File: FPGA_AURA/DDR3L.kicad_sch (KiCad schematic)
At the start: 58 parts, among them U500 MT41K128M16JT-125_IT_K

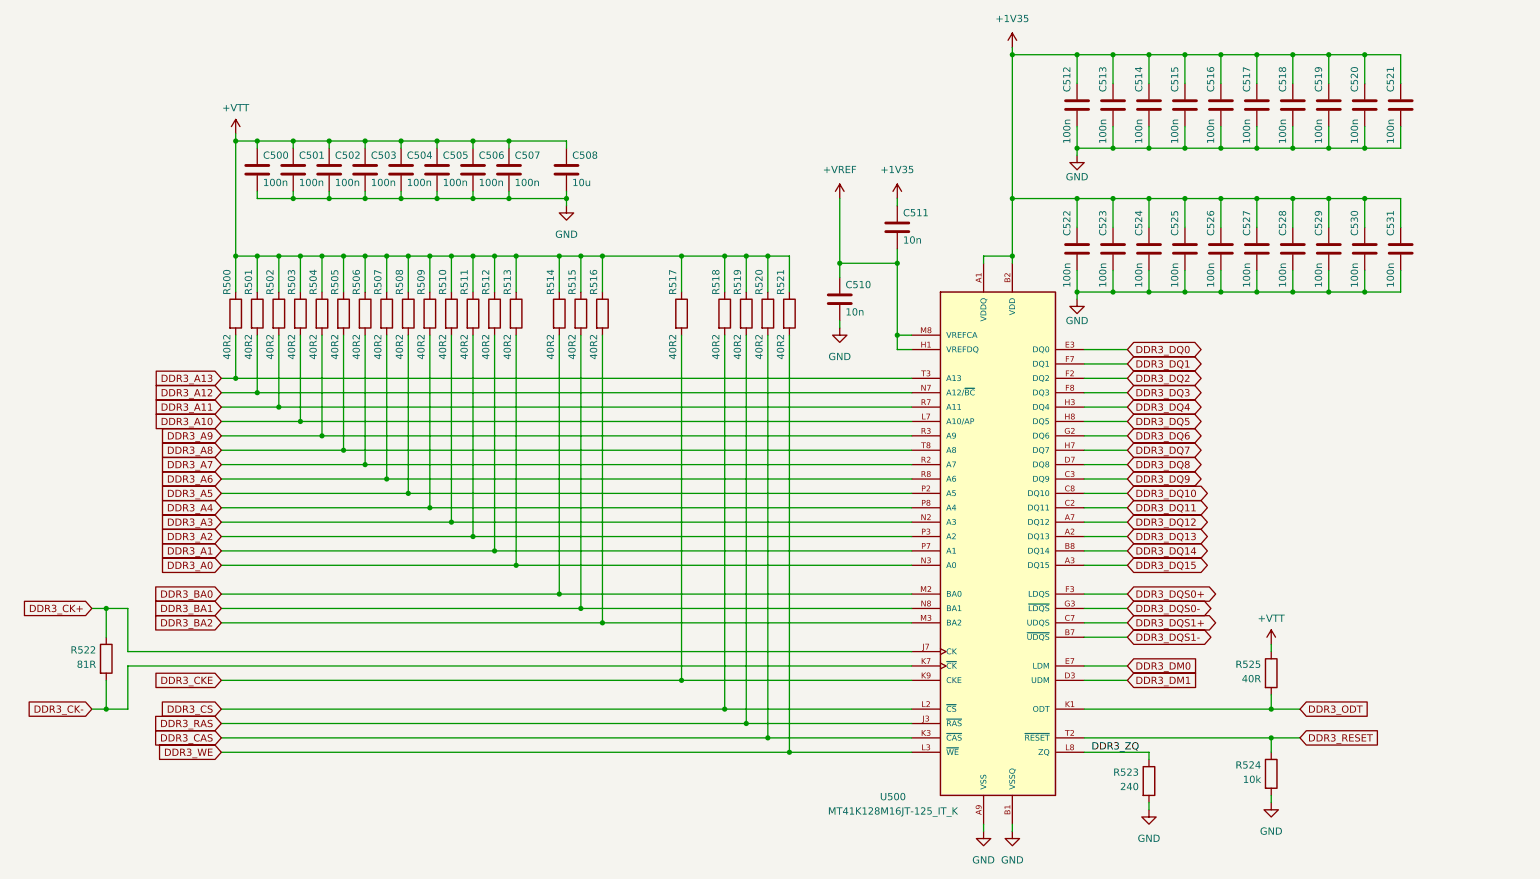
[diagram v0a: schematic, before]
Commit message: Following new DDR3 reference
Using Scopefun v2 as a reference design for the XC7A35T-FTG256
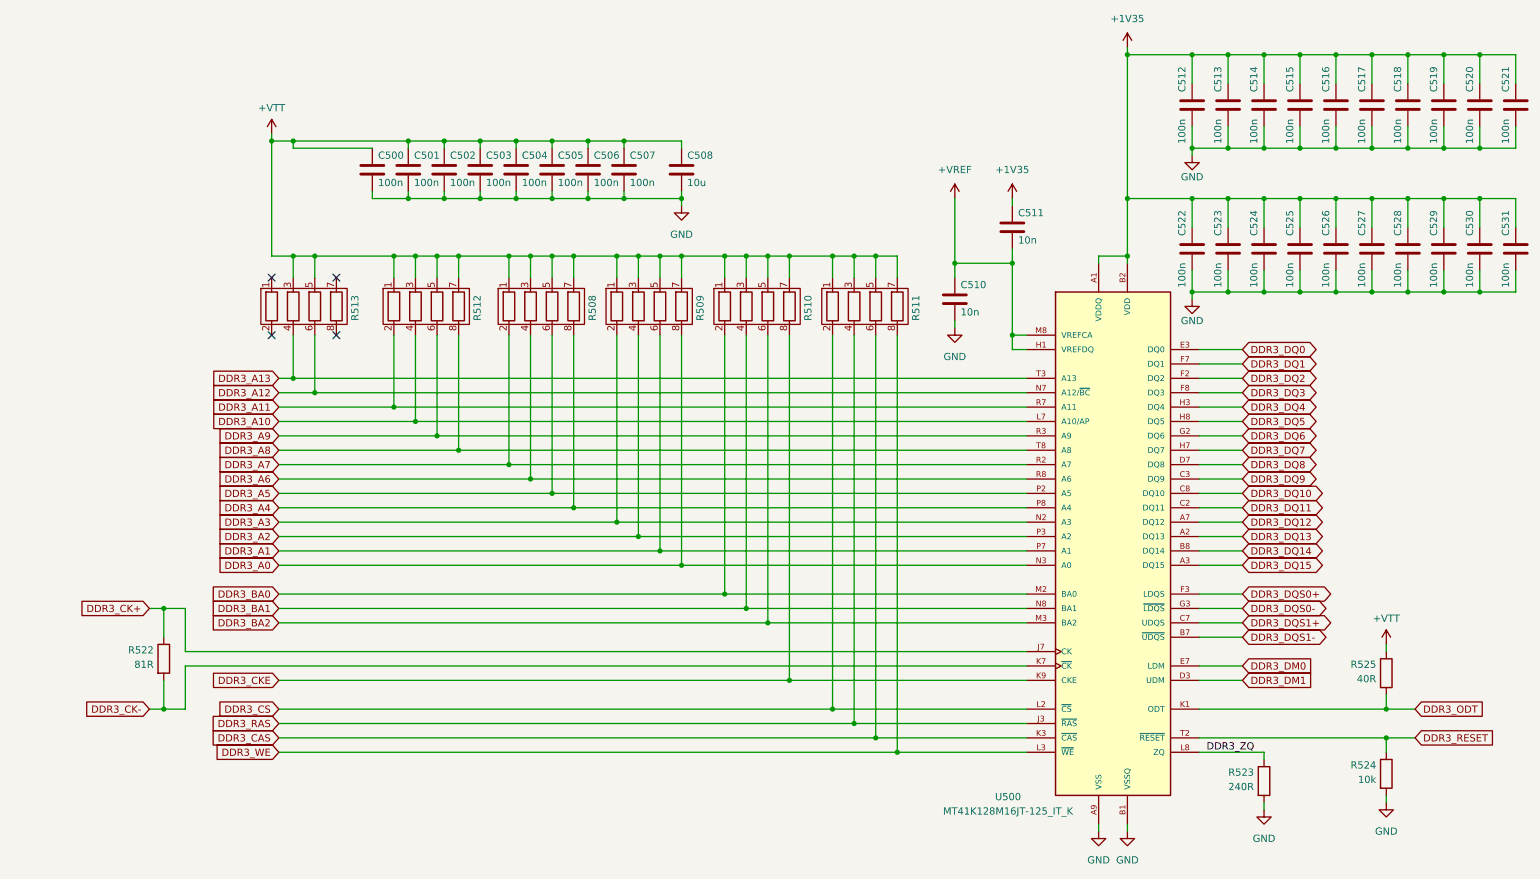
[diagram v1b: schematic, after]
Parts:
- removed R500, R501, R502, R503, R504, R505, R506, R507, R508, R509, R510, R511, R512, R513, R514, R515, R516, R517, R518, R519, R520, R521: 40R2, Resistor_SMD:R_0402_1005Metric, symbol Device:R
- added R508, R509, R510, R511, R512, R513: ~, YC124-FR-0740R2L:0402_4, symbol YC124-FR-0740R2L:R_Array
- R523: value 240 -> 240R
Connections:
- net +VTT: now also R508.1, R508.3, R508.5, R508.7, R509.1, R509.3, R509.5, R509.7, R510.1, R510.3, R510.5, R510.7, R511.1, R511.3, R511.5, R511.7, R512.1, R512.3, R512.5, R512.7, R513.3, R513.5
- net DDR3_A0: now also R509.8
- net DDR3_A1: now also R509.6
- net DDR3_A10: now also R512.4
- net DDR3_A11: now also R512.2
- net DDR3_A12: now also R513.6
- net DDR3_A13: now also R513.4
- net DDR3_A2: now also R509.4
- net DDR3_A3: now also R509.2
- net DDR3_A4: now also R508.8
- net DDR3_A5: now also R508.6
- net DDR3_A6: now also R508.4
- net DDR3_A7: now also R508.2
- net DDR3_A8: now also R512.8
- net DDR3_A9: now also R512.6
- net DDR3_BA0: now also R510.2
- net DDR3_BA1: now also R510.4
- net DDR3_BA2: now also R510.6
- net DDR3_CAS: now also R511.6
- net DDR3_CKE: now also R510.8
- net DDR3_CS: now also R511.2
- net DDR3_RAS: now also R511.4
- net DDR3_WE: now also R511.8
- no-connect marks 0 -> 4
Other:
- moved on the sheet: C500, C501, C502, C503, C504, C505, C506, C507, C508, C510, C511, C512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

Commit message: Moved to KiCAD V10 for delay.
The FPGA PCB has now been moved to KiCAD V10 to make use of the new delay features and design rules are being setup.

PCB stack-up has now been decided.
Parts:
- R508, R509, R510, R511, R512, R513: value ~ -> (none)

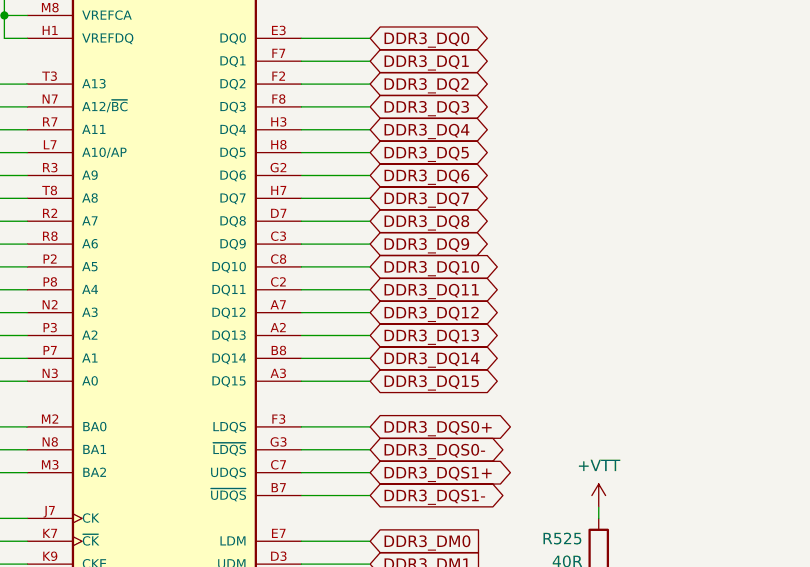
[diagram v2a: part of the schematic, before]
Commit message: Fixed delay matching issue and started data lines
The delay matching is now working again and the data byte lanes are in the process of being routed.
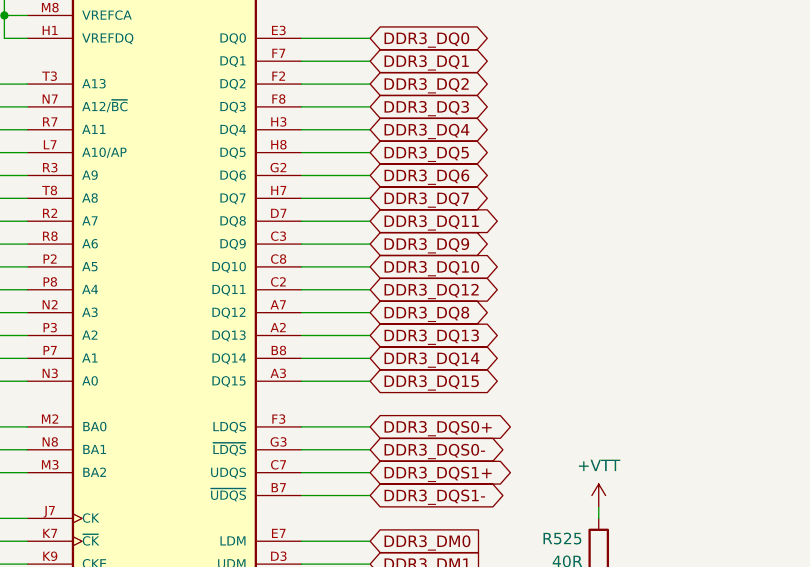
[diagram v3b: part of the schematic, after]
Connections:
- net DDR3_DQ11: now also U500.D7 (DQ8); no longer U500.C2 (DQ11)
- net DDR3_DQ12: now also U500.C2 (DQ11); no longer U500.A7 (DQ12)
- net DDR3_DQ8: now also U500.A7 (DQ12); no longer U500.D7 (DQ8)
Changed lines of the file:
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@@
-	(wire
-		(pts
-			(xy 231.14 93.98) (xy 223.52 93.98)
-		)
-		(stroke
-			(width 0)
-			(type default)
-		)
-	)
 	(wire
 		(pts
@@
 	(wire
 		(pts
+			(xy 223.52 93.98) (xy 231.14 93.98)
+		)
+		(stroke
+			(width 0)
+			(type default)
+		)
+	)
+	(wire
+		(pts
 			(xy 222.25 38.1) (xy 228.6 38.1)
 		)
@@
 	(wire
 		(pts
-			(xy 231.14 109.22) (xy 223.52 109.22)
-		)
-		(stroke
-			(width 0)
-			(type default)
-		)
-	)
-	(wire
-		(pts
 			(xy 158.75 57.15) (xy 158.75 60.96)
 		)
@@
 	(wire
 		(pts
+			(xy 223.52 109.22) (xy 231.14 109.22)
+		)
+		(stroke
+			(width 0)
+			(type default)
+		)
+	)
+	(wire
+		(pts
 			(xy 260.35 46.99) (xy 266.7 46.99)
 		)
@@
 	(wire
 		(pts
+			(xy 223.52 101.6) (xy 231.14 101.6)
+		)
+		(stroke
+			(width 0)
+			(type default)
+		)
+	)
+	(wire
+		(pts
 			(xy 231.14 78.74) (xy 223.52 78.74)
 		)
@@
 	(wire
 		(pts
-			(xy 231.14 104.14) (xy 223.52 104.14)
-		)
-		(stroke
-			(width 0)
-			(type default)
-		)
-	)
-	(wire
-		(pts
 			(xy 266.7 38.1) (xy 273.05 38.1)
 		)
@@
 	(wire
 		(pts
+			(xy 223.52 104.14) (xy 231.14 104.14)
+		)
+		(stroke
+			(width 0)
+			(type default)
+		)
+	)
+	(wire
+		(pts
 			(xy 234.95 153.67) (xy 234.95 154.94)
 		)
@@
 	(wire
 		(pts
-			(xy 231.14 101.6) (xy 223.52 101.6)
+			(xy 223.52 96.52) (xy 231.14 96.52)
 		)
 		(stroke
@@
 		(pts
 			(xy 190.5 58.42) (xy 190.5 71.12)
-		)
-		(stroke
-			(width 0)
-			(type default)
-		)
-	)
-	(wire
-		(pts
-			(xy 231.14 96.52) (xy 223.52 96.52)
 		)
 		(stroke
@@
 	(global_label "DDR3_DQ11"
 		(shape bidirectional)
+		(at 231.14 93.98 0)
+		(fields_autoplaced yes)
+		(effects
+			(font
+				(size 1.27 1.27)
+			)
+			(justify left)
+		)
+		(property "Intersheetrefs" "${INTERSHEET_REFS}"
+			(at 246.2431 93.98 0)
+			(hide yes)
+			(show_name no)
+			(do_not_autoplace no)
+			(effects
+				(font
+					(size 1.27 1.27)
+				)
+				(justify left)
+			)
+		)
+	)
+	(global_label "DDR3_DQ10"
+		(shape bidirectional)
+		(at 231.14 99.06 0)
+		(fields_autoplaced yes)
+		(effects
+			(font
+				(size 1.27 1.27)
+			)
+			(justify left)
+		)
+		(property "Intersheetrefs" "${INTERSHEET_REFS}"
+			(at 246.2431 99.06 0)
+			(hide yes)
+			(show_name no)
+			(do_not_autoplace no)
+			(effects
+				(font
+					(size 1.27 1.27)
+				)
+				(justify left)
+			)
+		)
+	)
+	(global_label "DDR3_BA2"
+		(shape input)
+		(at 60.96 121.92 180)
+		(fields_autoplaced yes)
+		(effects
+			(font
+				(size 1.27 1.27)
+			)
+			(justify right)
+		)
+		(property "Intersheetrefs" "${INTERSHEET_REFS}"
+			(at 48.4196 121.92 0)
+			(hide yes)
+			(show_name no)
+			(do_not_autoplace no)
+			(effects
+				(font
+					(size 1.27 1.27)
+				)
+				(justify right)
+			)
+		)
+	)
+	(global_label "DDR3_DQ15"
+		(shape bidirectional)
+		(at 231.14 111.76 0)
+		(fields_autoplaced yes)
+		(effects
+			(font
+				(size 1.27 1.27)
+			)
+			(justify left)
+		)
+		(property "Intersheetrefs" "${INTERSHEET_REFS}"
+			(at 246.2431 111.76 0)
+			(hide yes)
+			(show_name no)
+			(do_not_autoplace no)
+			(effects
+				(font
+					(size 1.27 1.27)
+				)
+				(justify left)
+			)
+		)
+	)
+	(global_label "DDR3_DQ12"
+		(shape bidirectional)
 		(at 231.14 101.6 0)
 		(fields_autoplaced yes)
@@
 		)
 	)
-	(global_label "DDR3_DQ10"
-		(shape bidirectional)
-		(at 231.14 99.06 0)
-		(fields_autoplaced yes)
-		(effects
-			(font
-				(size 1.27 1.27)
-			)
-			(justify left)
-		)
-		(property "Intersheetrefs" "${INTERSHEET_REFS}"
-			(at 246.2431 99.06 0)
-			(hide yes)
-			(show_name no)
-			(do_not_autoplace no)
-			(effects
-				(font
-					(size 1.27 1.27)
-				)
-				(justify left)
-			)
-		)
-	)
-	(global_label "DDR3_BA2"
-		(shape input)
-		(at 60.96 121.92 180)
-		(fields_autoplaced yes)
-		(effects
-			(font
-				(size 1.27 1.27)
-			)
-			(justify right)
-		)
-		(property "Intersheetrefs" "${INTERSHEET_REFS}"
-			(at 48.4196 121.92 0)
-			(hide yes)
-			(show_name no)
-			(do_not_autoplace no)
-			(effects
-				(font
-					(size 1.27 1.27)
-				)
-				(justify right)
-			)
-		)
-	)
-	(global_label "DDR3_DQ15"
-		(shape bidirectional)
-		(at 231.14 111.76 0)
-		(fields_autoplaced yes)
-		(effects
-			(font
-				(size 1.27 1.27)
-			)
-			(justify left)
-		)
-		(property "Intersheetrefs" "${INTERSHEET_REFS}"
-			(at 246.2431 111.76 0)
-			(hide yes)
-			(show_name no)
-			(do_not_autoplace no)
-			(effects
-				(font
-					(size 1.27 1.27)
-				)
-				(justify left)
-			)
-		)
-	)
-	(global_label "DDR3_DQ12"
-		(shape bidirectional)
-		(at 231.14 104.14 0)
-		(fields_autoplaced yes)
-		(effects
-			(font
-				(size 1.27 1.27)
-			)
-			(justify left)
-		)
-		(property "Intersheetrefs" "${INTERSHEET_REFS}"
-			(at 246.2431 104.14 0)
-			(hide yes)
-			(show_name no)
-			(do_not_autoplace no)
-			(effects
-				(font
-					(size 1.27 1.27)
-				)
-				(justify left)
-			)
-		)
-	)
 	(global_label "DDR3_RAS"
 		(shape input)
@@
 	(global_label "DDR3_DQ8"
 		(shape bidirectional)
-		(at 231.14 93.98 0)
+		(at 231.14 104.14 0)
 		(fields_autoplaced yes)
 		(effects
@@
 		)
 		(property "Intersheetrefs" "${INTERSHEET_REFS}"
-			(at 245.0336 93.98 0)
+			(at 245.0336 104.14 0)
 			(hide yes)
 			(show_name no)

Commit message: Continuing the FTDI
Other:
- moved on the sheet: C500, C501, C502, C503, C504, C505, C506, C507, C508, C510, C511, C512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
